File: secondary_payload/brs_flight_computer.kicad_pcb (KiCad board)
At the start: 2 copper layers, 81.1 x 75 mm, 6 parts, among them J1 Conn_01x06_Male, J2 Conn_01x06_Male, J3 Conn_01x10_Male, J4 Conn_01x16_Male, J5 Conn_01x03_Male, J6 Conn_01x12_Male

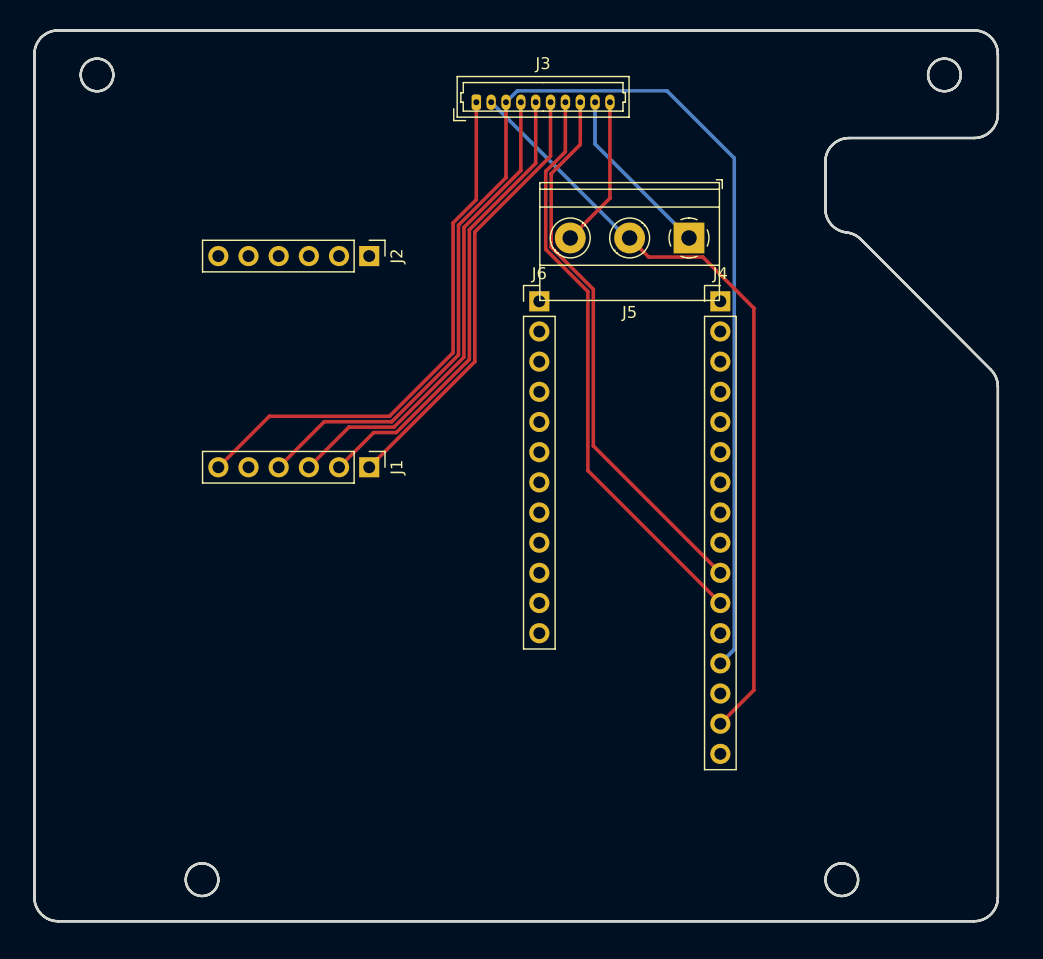
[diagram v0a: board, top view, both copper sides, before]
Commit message: Updating based on harnesses
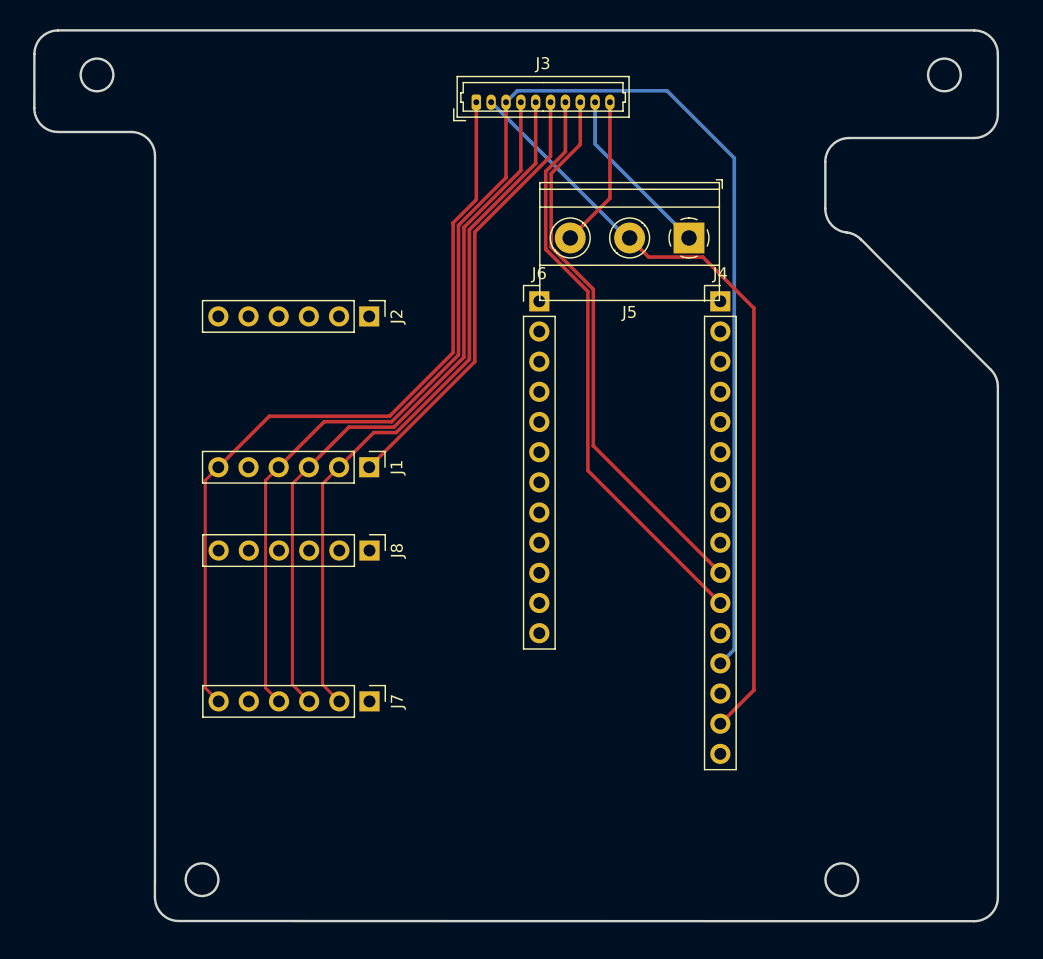
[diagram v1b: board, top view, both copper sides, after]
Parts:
- added J7: Conn_01x06_Male, Connector_PinHeader_2.54mm:PinHeader_1x06_P2.54mm_Vertical, F.Cu at (137.3, 127.7)
- added J8: Conn_01x06_Male, Connector_PinHeader_2.54mm:PinHeader_1x06_P2.54mm_Vertical, F.Cu at (137.3, 115.0)
- moved J2 5.08 mm to (137.3, 95.2)
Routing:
- net /SCL: track 40.3 -> 61.2 mm
- net /SDA: track 38.7 -> 59.6 mm
- net GND: track 107.0 -> 127.6 mm
- net VDDF: track 45.7 -> 66.3 mm
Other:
- outline, holes or cut-outs redrawn

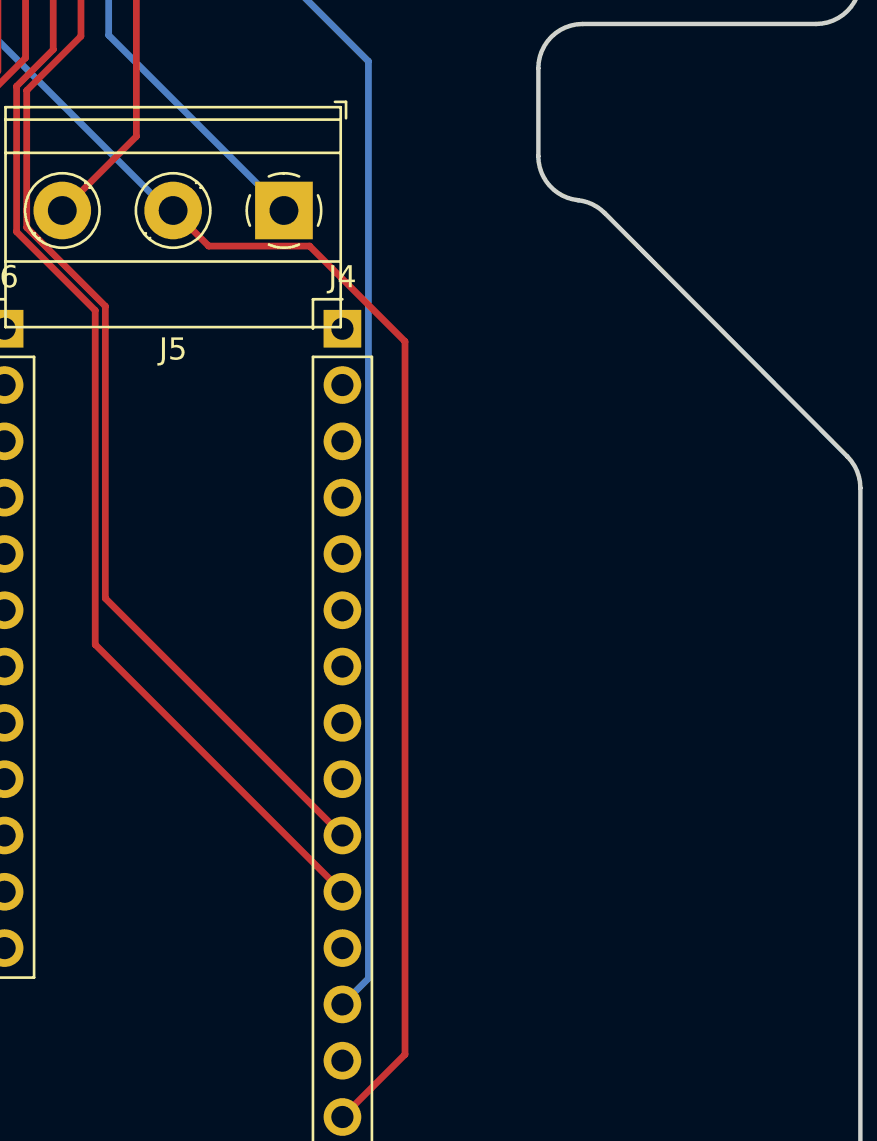
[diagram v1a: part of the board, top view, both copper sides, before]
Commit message: Integrating flight computer
- EPS commands tested and working
- Updated v3, fixing connector polarity
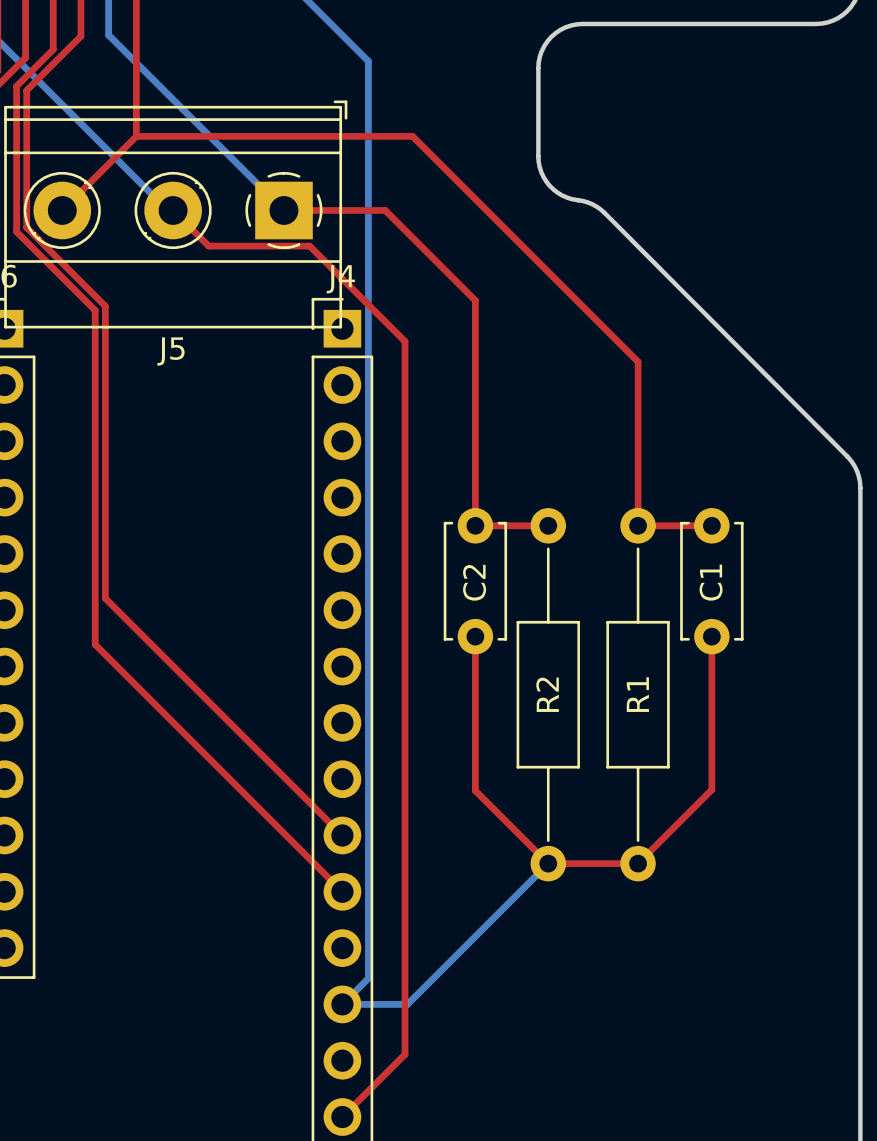
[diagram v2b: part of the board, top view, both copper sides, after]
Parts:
- added C1: C, Capacitor_THT:C_Disc_D5.0mm_W2.5mm_P5.00mm, F.Cu at (183.5, 102.9)
- added C2: C, Capacitor_THT:C_Disc_D5.0mm_W2.5mm_P5.00mm, F.Cu at (172.8, 102.9)
- added R1: R, Resistor_THT:R_Axial_DIN0207_L6.3mm_D2.5mm_P15.24mm_Horizontal, F.Cu at (180.2, 102.9)
- added R2: R, Resistor_THT:R_Axial_DIN0207_L6.3mm_D2.5mm_P15.24mm_Horizontal, F.Cu at (176.1, 102.9)
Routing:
- net GND: track 127.6 -> 166.8 mm
- net /NC_V: track 12.8 -> 50.4 mm
- net /NO_V: track 14.7 -> 38.5 mm

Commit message: Integrating flight computer
- Update FSS100 connector
- Update secondary payload connector
- Add pullup resistor to GaAs data
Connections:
- J3 pad 1: VDDF -> /NC_V
- J3 pad 10: /NC_V -> VDDF
- J3 pad 2: VPP -> /NO_V
- J3 pad 3: GND -> /UNSET
- J3 pad 4: /SCL -> /SET
- J3 pad 5: /SDA -> /MAG_INT
- J3 pad 6: /MAG_INT -> /SDA
- J3 pad 7: /SET -> /SCL
- J3 pad 8: /UNSET -> GND
- J3 pad 9: /NO_V -> VPP
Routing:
- net VDDF: track 66.3 -> 85.7 mm
- net /NO_V: track 38.5 -> 53.9 mm
- net /MAG_INT: track 37.1 -> 52.3 mm
- net /SDA: track 59.6 -> 66.1 mm
- net GND: track 166.8 -> 160.3 mm
- net VPP: track 65.5 -> 61.7 mm
- net /SET: track 48.9 -> 50.7 mm
- net /SCL: track 61.2 -> 60.5 mm
- net /UNSET: track 46.5 -> 47.1 mm

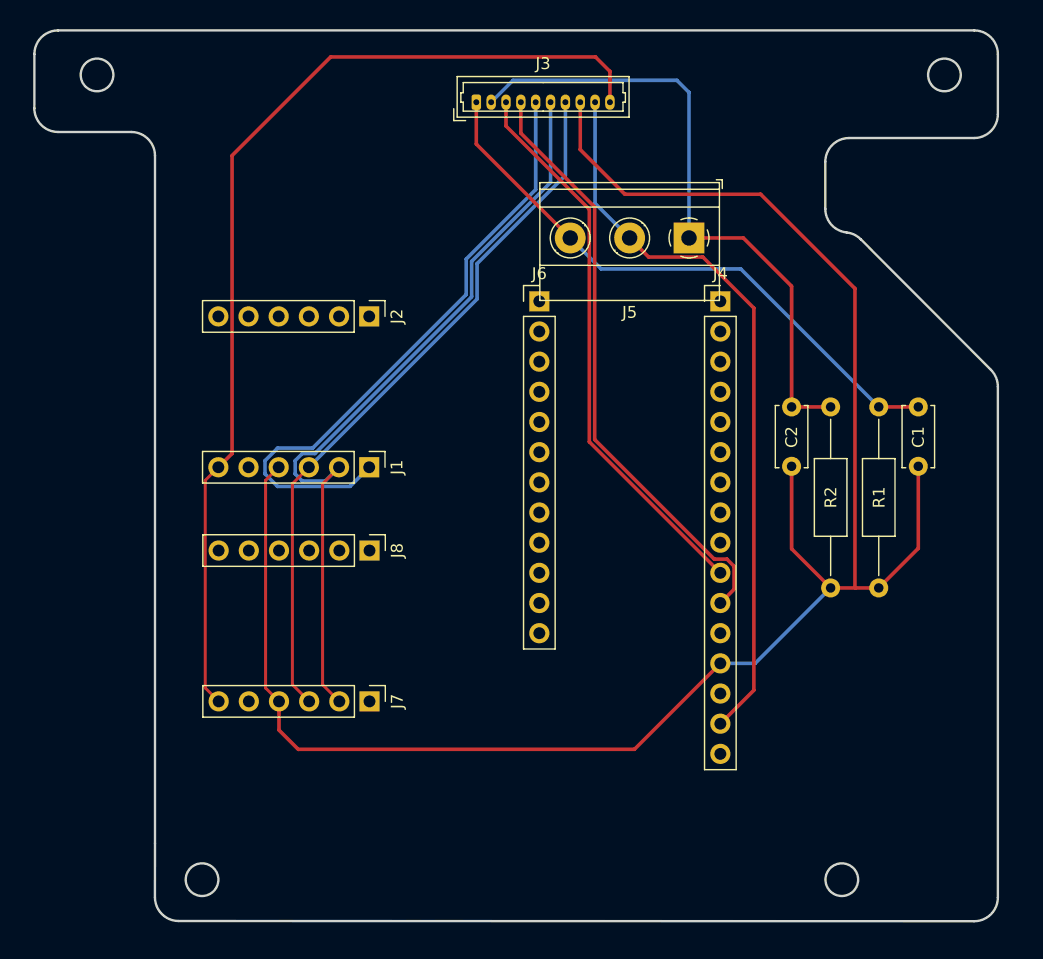
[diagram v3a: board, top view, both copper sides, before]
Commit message: Finished PCBs
- Finished flight computer
- Finished payload holder
- Finished contact board
- Ordered everything
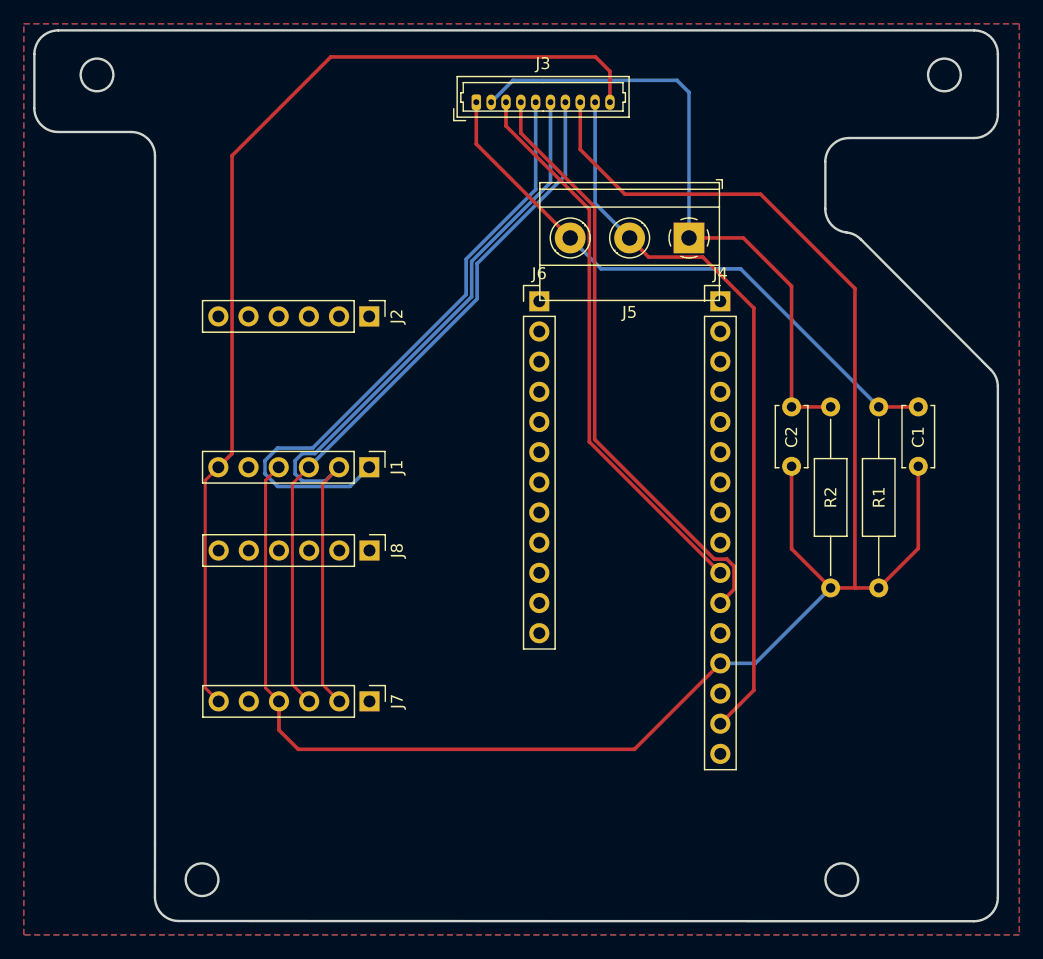
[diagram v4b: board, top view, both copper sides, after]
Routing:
- added copper zone on B.Cu, net (none)
- added copper zone on F.Cu, net GND
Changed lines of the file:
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@@
   )
   (setup
-    (last_trace_width 0.3048)
+    (last_trace_width 0.1524)
     (user_trace_width 0.1524)
     (user_trace_width 0.254)
@@
       (excludeedgelayer true)
       (linewidth 0.100000)
-      (plotframeref false)
+      (plotframeref true)
       (viasonmask false)
       (mode 1)
@@
       (padsonsilk false)
       (subtractmaskfromsilk false)
-      (outputformat 1)
+      (outputformat 4)
       (mirror false)
       (drillshape 0)
       (scaleselection 1)
-      (outputdirectory "Gerbers"))
+      (outputdirectory "Renders"))
   )
   (net 0 "")
@@
   (segment (start 166.340791 115.685199) (end 167.403305 115.685199) (width 0.3048) (layer F.Cu) (net 17))
   (segment (start 156.273011 105.617419) (end 166.340791 115.685199) (width 0.3048) (layer F.Cu) (net 17))
+  (zone (net 1) (net_name GND) (layer F.Cu) (hatch edge 0.508)
+    (connect_pads (clearance 0.254))
+    (min_thickness 0.254)
+    (fill yes (arc_segments 32) (thermal_gap 0.508) (thermal_bridge_width 0.508))
+    (polygon
+      (pts
+        (xy 192.024 147.32) (xy 108.204 147.32) (xy 108.204 70.612) (xy 192.024 70.612)
+      )
+    )
+  )
+  (zone (net 0) (net_name "") (layer B.Cu) (hatch edge 0.508)
+    (connect_pads (clearance 0.254))
+    (min_thickness 0.254)
+    (fill yes (arc_segments 32) (thermal_gap 0.508) (thermal_bridge_width 0.508))
+    (polygon
+      (pts
+        (xy 192.024 147.32) (xy 108.204 147.32) (xy 108.204 70.612) (xy 192.024 70.612)
+      )
+    )
+  )
 )

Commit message: Update flight computer
- Add exposed pad to microcontroller
- Update flight computer firmware
- Update secondary payload outline
- Order boards
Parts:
- C1, C2: footprint Capacitor_THT:C_Disc_D5.0mm_W2.5mm_P5.00mm -> Capacitor_SMD:C_0603_1608Metric
- R1, R2: footprint Resistor_THT:R_Axial_DIN0207_L6.3mm_D2.5mm_P15.24mm_Horizontal -> Resistor_SMD:R_0603_1608Metric
- moved C1 36.2 mm to (154.2, 81.7), turned to 90 degrees
- moved R1 32.3 mm to (155.8, 81.7), turned to 90 degrees
- moved R2 25.2 mm to (162.6, 81.7), turned to 90 degrees
- moved C2 22.9 mm to (164.2, 81.7), turned to 90 degrees
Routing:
- net GND: track 160.3 -> 63.9 mm, vias 0 -> 1
- net /NC_V: track 49.9 -> 22.6 mm
- net /NO_V: track 53.9 -> 38.0 mm
- net /UNSET: track 47.1 -> 59.7 mm
- net /SET: track 50.7 -> 52.6 mm
- added copper zone on B.Cu, net GND
- removed copper zone on B.Cu, net (none)
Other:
- outline, holes or cut-outs redrawn
